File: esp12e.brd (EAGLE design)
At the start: 50 x 50 mm, 32 parts, among them IC1 117\33

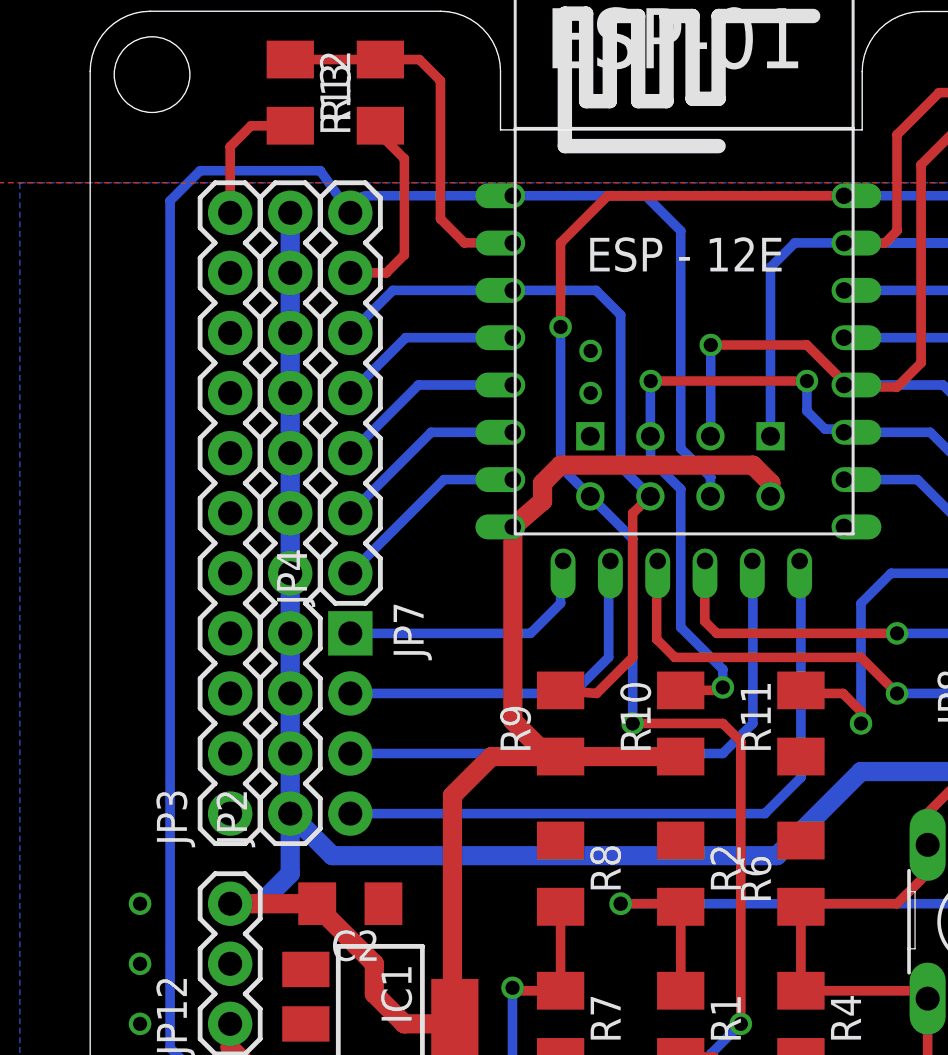
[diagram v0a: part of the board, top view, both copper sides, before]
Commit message: ISP AVR header - may be changed again
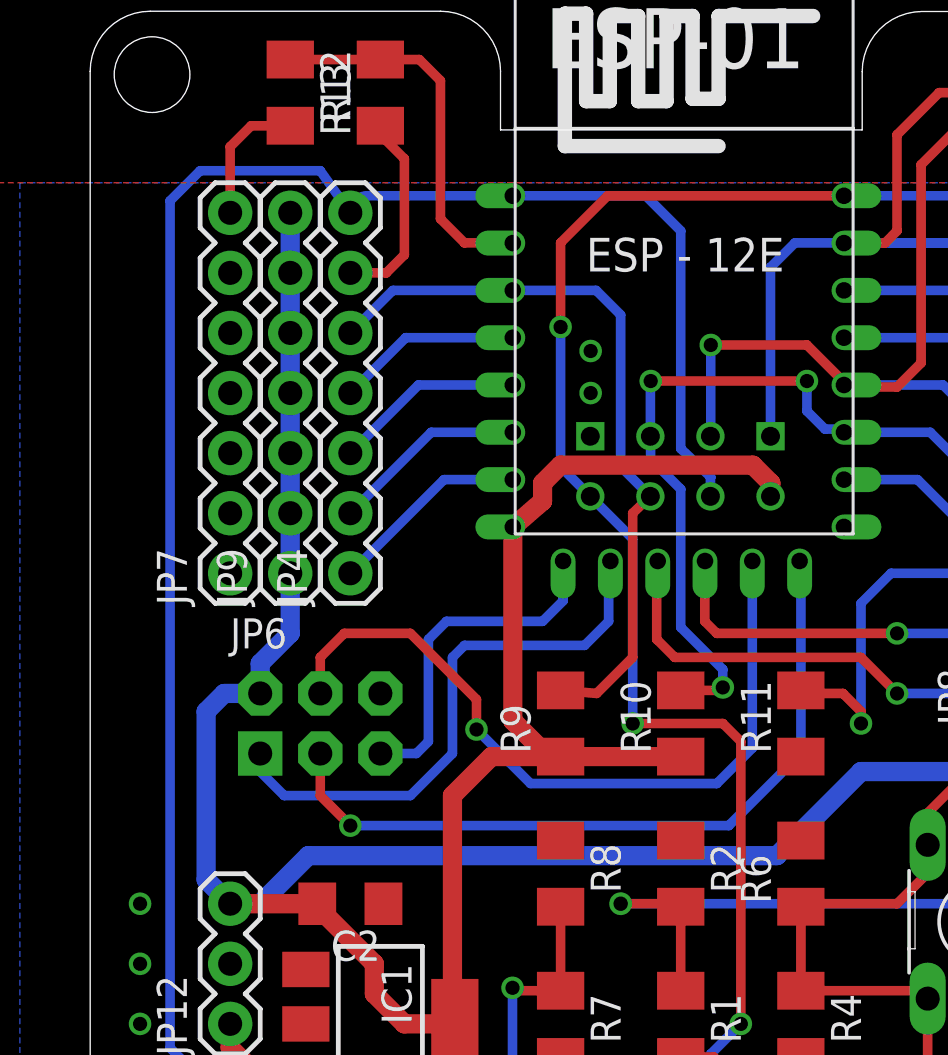
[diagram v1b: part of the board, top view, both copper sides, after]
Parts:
- removed JP2, JP3: M11PTH, SparkFun-Connectors:1X11
- added JP6: AVR_SPI_PRG_6NS, SparkFun-Connectors:2X3-NS
- added JP9: (no value), SparkFun-Connectors:1X07
- JP7: device SparkFun-Connectors:1X04_NO_SILK -> SparkFun-Connectors:1X07
- moved JP7 5.68 mm to (6.35, 26.7), turned to 90 degrees
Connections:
- net +3V3: now also JP6.2, JP9.1, JP9.2, JP9.3, JP9.4, JP9.5, JP9.6, JP9.7; no longer JP2.1, JP2.10, JP2.11, JP2.2, JP2.3, JP2.4, JP2.5, JP2.6, JP2.7, JP2.8, JP2.9
- net GND: now also JP6.6, JP7.1, JP7.2, JP7.3, JP7.4, JP7.5, JP7.6, JP7.7; no longer JP3.1, JP3.10, JP3.11, JP3.2, JP3.3, JP3.4, JP3.5, JP3.6, JP3.7, JP3.8, JP3.9
- net N$10: now also JP6.1, U$3.MISO; no longer JP7.1, U$3.CS0
- net N$11: now also JP6.4, U$3.MOSI; no longer JP7.2, U$3.MISO
- net N$12: now also JP6.3, U$3.SCLK; no longer JP7.3, U$3.MOSI
- net N$13: now also JP6.5, U$3.CS0; no longer JP7.4, U$3.SCLK
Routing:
- net N$11: track 15.7 -> 32.1 mm, vias 0 -> 1
- net N$13: track 28.9 -> 14.6 mm
- net N$10: track 11.2 -> 23.9 mm
- net N$12: track 24.4 -> 32.0 mm, vias 0 -> 1
- net +3V3: track 167.8 -> 171.5 mm

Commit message: hackaday swag
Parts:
- JP6: value AVR_SPI_PRG_6NS -> AVR_SPI
- moved JP12 0.25 mm to (6.60, 7.62)
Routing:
- net GPIO15: track 24.1 -> 22.3 mm
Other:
- outline, holes or cut-outs redrawn
- board text added: "3V3"
- board text added: "5V"
- board text added: "ADC"
- board text added: "CHPD"
- board text added: "GND"
- board text added: "IO00"
- board text added: "IO02"
- board text added: "IO04"
- board text added: "IO05"
- board text added: "IO09*"
- board text added: "IO10*"
- board text added: "IO12"
- board text added: "IO13"
- board text added: "IO14"
- board text added: "IO15"
- board text added: "IO16"
- board text added: "RST"
- board text added: "RX"
- board text added: "TX"

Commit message: 100nF because of regulator
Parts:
- C1: value 10uF -> 100nF
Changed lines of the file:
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@@
 <attribute name="VALUE" x="13.2588" y="4.826" size="1.27" layer="25" font="vector" rot="R90"/>
 </element>
-<element name="C1" library="resistor" package="C1206" value="10uF" x="11.43" y="2.54" smashed="yes">
+<element name="C1" library="resistor" package="C1206" value="100nF" x="11.43" y="2.54" smashed="yes">
 <attribute name="NAME" x="5.08" y="2.667" size="1.27" layer="25" font="vector"/>
 <attribute name="VALUE" x="5.08" y="0.889" size="1.27" layer="25" font="vector"/>
